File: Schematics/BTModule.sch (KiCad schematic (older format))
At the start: 9 parts, among them U4 CSRA64215

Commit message: Fixed CDC interface schematic; Fixed SPDIF output interface schematic; Added screw terminals; Modified PCB design
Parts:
- R7: footprint Resistor_THT:R_Axial_DIN0207_L6.3mm_D2.5mm_P10.16mm_Horizontal -> Resistor_THT:R_Axial_DIN0309_L9.0mm_D3.2mm_P12.70mm_Horizontal
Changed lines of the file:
@@
 F 0 "R7" V 4193 2350 50  0000 C CNN
 F 1 "10k" V 4284 2350 50  0000 C CNN
-F 2 "Resistor_THT:R_Axial_DIN0207_L6.3mm_D2.5mm_P10.16mm_Horizontal" V 4330 2350 50  0001 C CNN
+F 2 "Resistor_THT:R_Axial_DIN0309_L9.0mm_D3.2mm_P12.70mm_Horizontal" V 4330 2350 50  0001 C CNN
 F 3 "~" H 4400 2350 50  0001 C CNN
 	1    4400 2350

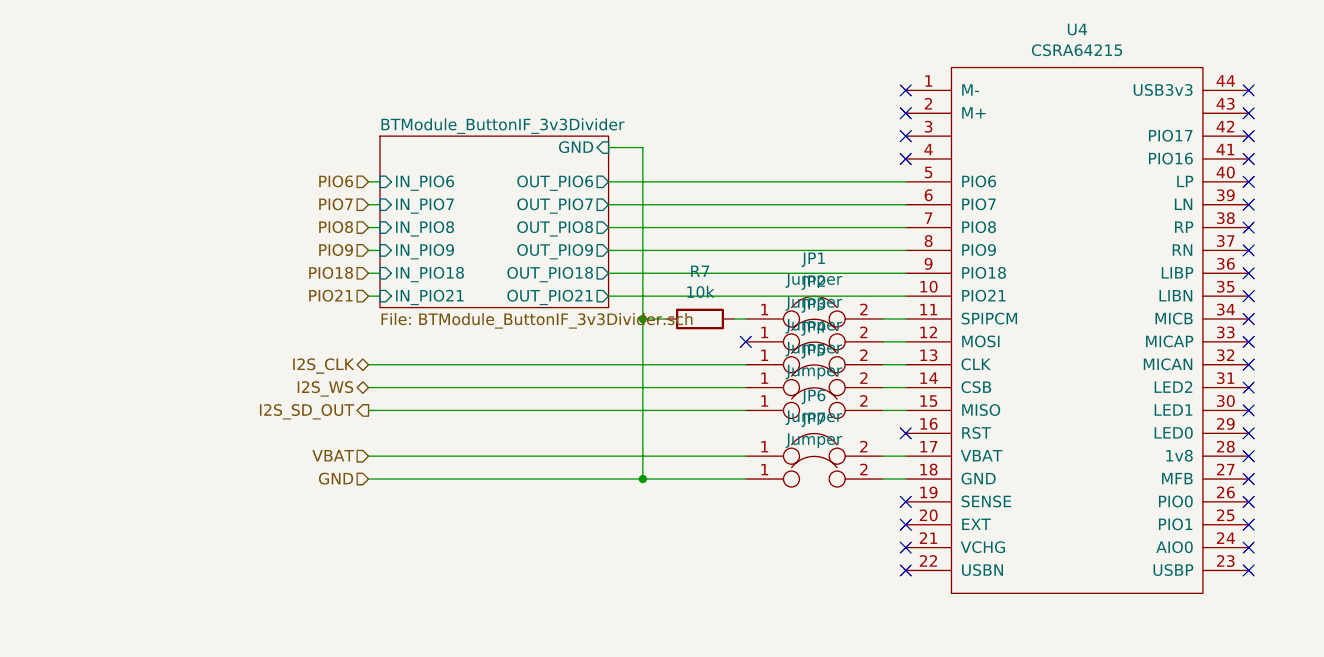
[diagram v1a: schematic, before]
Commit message: Fixed voltage level issues between BT module and WM8804; fixed CDC Emulator hw interface; modified PCB design
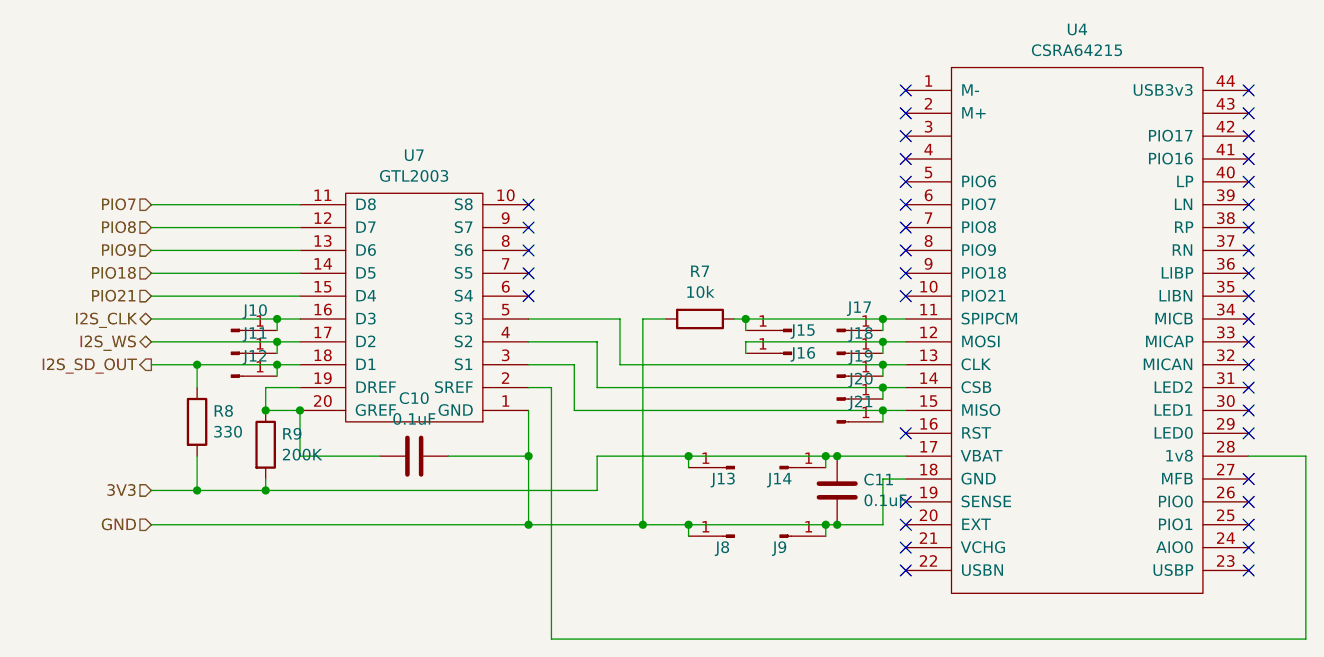
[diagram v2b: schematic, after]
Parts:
- removed JP1, JP2, JP3, JP4, JP5, JP6, JP7: Jumper, Connector_PinHeader_2.54mm:PinHeader_1x02_P2.54mm_Vertical, symbol Device:Jumper
- added C10, C11: 0.1uF, Capacitor_THT:C_Disc_D5.0mm_W2.5mm_P2.50mm, symbol Device:C
- added J10, J11, J12, J13, J14, J15, J16, J17, J18, J19, J20, J21, J8, J9: Conn_01x01_Male, Connector_PinHeader_2.54mm:PinHeader_1x01_P2.54mm_Vertical, symbol Connector:Conn_01x01_Male
- added R8: 330, Resistor_THT:R_Axial_DIN0204_L3.6mm_D1.6mm_P2.54mm_Vertical, symbol Device:R
- added R9: 200K, Resistor_THT:R_Axial_DIN0204_L3.6mm_D1.6mm_P5.08mm_Vertical, symbol Device:R
- added U7: GTL2003, GTL2003:GTL2003, symbol GTL2003:GTL2003
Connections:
- net GND: now also U4.18 (GND), C10.1, C11.2, J8.1 (Pin_1), J9.1 (Pin_1), U7.1 (GND)
- net I2S_CLK: now also J10.1 (Pin_1), U7.16 (D3)
- net I2S_SD_OUT: now also J12.1 (Pin_1), R8.1, U7.18 (D1)
- net I2S_WS: now also J11.1 (Pin_1), U7.17 (D2)
- net PIO18: now also U7.14 (D5)
- net PIO21: now also U7.15 (D4)
- net PIO7: now also U7.11 (D8)
- net PIO8: now also U7.12 (D7)
- net PIO9: now also U7.13 (D6)
- net at U4.11 (SPIPCM): now also R7.1, J15.1 (Pin_1), J17.1 (Pin_1)
- net at U4.12 (MOSI): now also J16.1 (Pin_1), J18.1 (Pin_1)
- net at U4.13 (CLK): now also J19.1 (Pin_1), U7.5 (S3)
- net at U4.14 (CSB): now also J20.1 (Pin_1), U7.4 (S2)
- net at U4.15 (MISO): now also J21.1 (Pin_1), U7.3 (S1)
- net 3V3: now reaches U4.17 (VBAT)
- net 3V3: now also C11.1, J13.1 (Pin_1), J14.1 (Pin_1), R8.2, R9.2
- net at U4.28 (1v8): now also U7.2 (SREF)
- net BTModule_ButtonIF_3v3Divider/OUT_PIO18: no longer names the net of U4.9 (PIO18)
- net BTModule_ButtonIF_3v3Divider/OUT_PIO21: no longer names the net of U4.10 (PIO21)
- net BTModule_ButtonIF_3v3Divider/OUT_PIO6: no longer names the net of U4.5 (PIO6)
- net BTModule_ButtonIF_3v3Divider/OUT_PIO7: no longer names the net of U4.6 (PIO7)
- net BTModule_ButtonIF_3v3Divider/OUT_PIO8: no longer names the net of U4.7 (PIO8)
- net BTModule_ButtonIF_3v3Divider/OUT_PIO9: no longer names the net of U4.8 (PIO9)
- new net: C10.2, R9.1, U7.19 (DREF), U7.20 (GREF)
- no-connect marks 32 -> 41
